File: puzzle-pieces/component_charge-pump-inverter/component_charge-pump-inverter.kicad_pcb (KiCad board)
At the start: 2 copper layers, 80 x 40 mm, 11 parts, among them J1 Conn_01x02_Pin, J2 Conn_01x02_Pin, J3 Conn_01x02_Pin

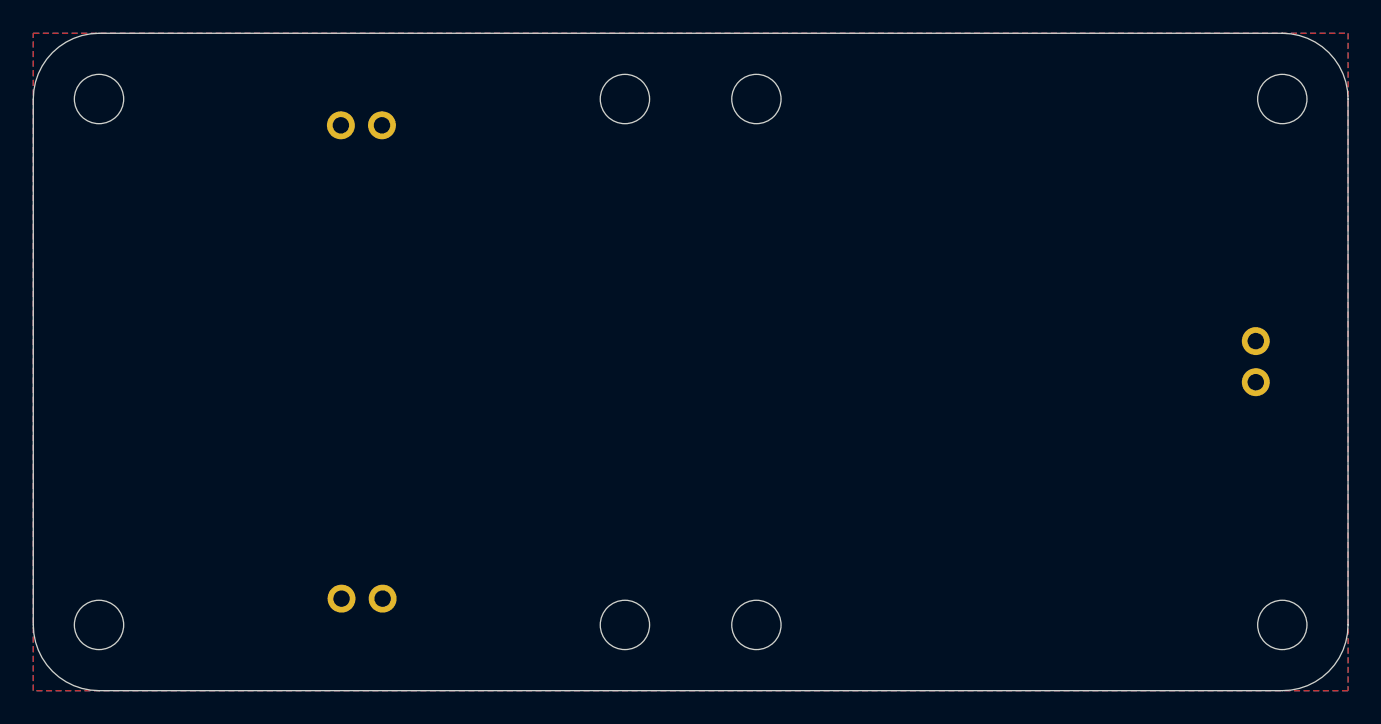
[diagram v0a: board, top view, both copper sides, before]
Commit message: Update PCB storage and inverter component files
Modified STEP and FreeCAD files for PCB storage system, updated .gitignore to include new backup patterns, and replaced charge-pump inverter KiCad files with new versions and documentation. Added PNG renders and a ZIP archive for the inverter component, reflecting a redesign or migration of project files.
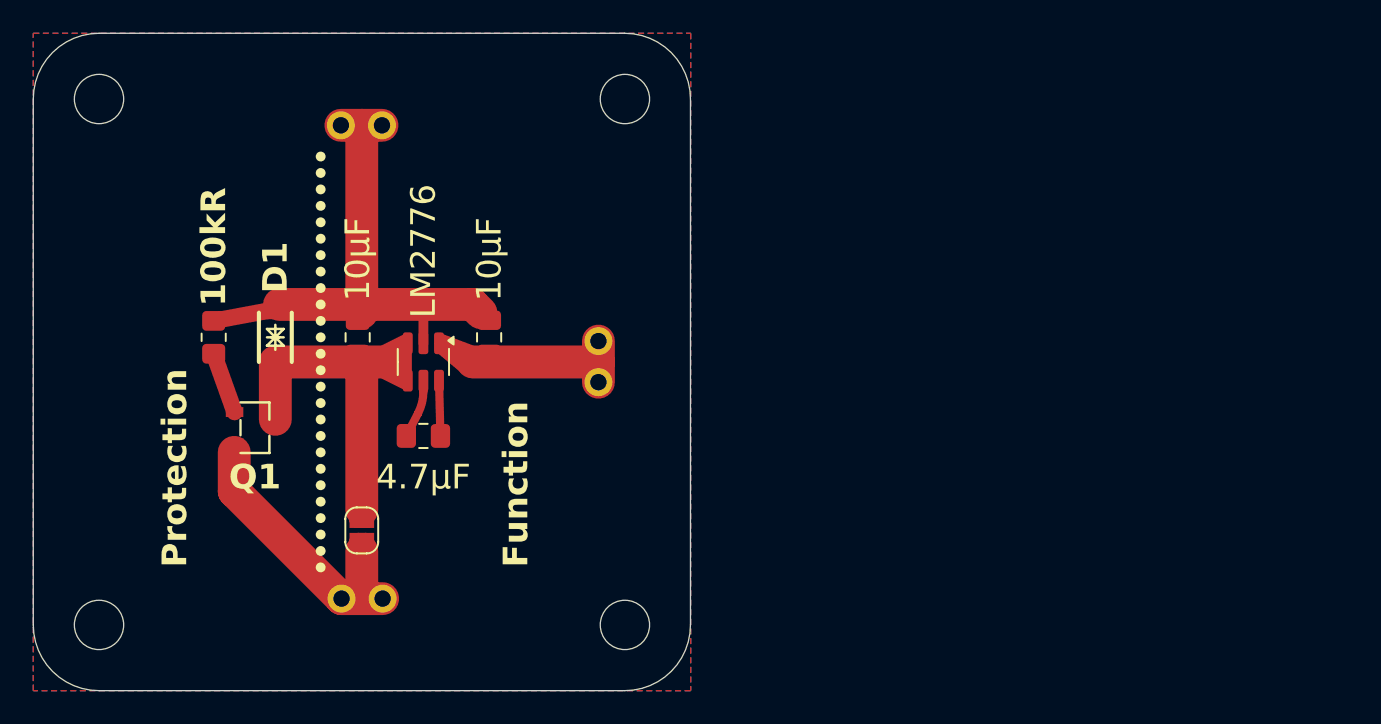
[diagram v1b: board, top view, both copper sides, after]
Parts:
- removed H1, H2, H3, H4: MH M3, EASYEDA2KICAD:MountingHole_3.0mm_M3_tight
- added C1: 4.7µF, Capacitor_SMD:C_0805_2012Metric_Pad1.18x1.45mm_HandSolder, F.Cu at (36.2, 37.0)
- added C2: 10µF, Capacitor_SMD:C_0805_2012Metric_Pad1.18x1.45mm_HandSolder, F.Cu at (40.2, 31.0)
- added C3: 10µF, Capacitor_SMD:C_0805_2012Metric_Pad1.18x1.45mm_HandSolder, F.Cu at (32.2, 31.0)
- added D1: SMF6.0CA, EASYEDA2KICAD:SOD-123FL_L2.8-W1.8-LS3.7-BI, F.Cu at (27.2, 31.0)
- added JP1: SolderJumper_2_Open, Jumper:SolderJumper-2_P1.3mm_Open_RoundedPad1.0x1.5mm, F.Cu at (32.5, 42.8)
- added Q1: AO3401A, EASYEDA2KICAD:SOT-23-3_L2.9-W1.6-P1.90-LS2.8-BR, F.Cu at (26.0, 36.5)
- added R1: 100kR, Resistor_SMD:R_0805_2012Metric_Pad1.20x1.40mm_HandSolder, F.Cu at (23.5, 31.0)
- added U1: LM2776, Package_TO_SOT_SMD:SOT-23-6, F.Cu at (36.2, 32.5)
- moved J3 56.4 mm to (32.5, 18.0), turned to 90 degrees
- moved J1 29.0 mm to (32.5, 47.0), turned to -90 degrees
- moved J2 20.5 mm to (47.0, 32.5), turned to 0 degrees
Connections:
- J2 pad 1: unconnected-(J2-Pin_1-Pad1) -> Net-(J2-Pin_1)
- J2 pad 2: unconnected-(J2-Pin_2-Pad2) -> Net-(J2-Pin_1)
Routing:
- net Net-(J3-Pin_1): track 0.00 -> 32.5 mm
- net Net-(JP1-B): track 0.00 -> 21.6 mm
- net Net-(J1-Pin_1): track 0.00 -> 17.0 mm
- net Net-(J2-Pin_1): track 0.00 -> 12.5 mm
- net Net-(Q1-G): track 0.00 -> 3.77 mm
- net Net-(U1-C1+): track 0.00 -> 3.58 mm
- net Net-(U1-C1-): track 0.00 -> 3.36 mm
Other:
- board size 80 x 40 mm -> 40 x 40 mm
- board text added: "Charge Pump"
- board text added: "Function"
- board text added: "GND"
- board text added: "Protection"
- board text removed: "0 V"
- board text removed: "Charge Pump Inverter"
